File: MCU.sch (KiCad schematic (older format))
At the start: 36 parts, among them Q1 BSS138, SW1 SW_Push, U2 STM32F722RETx

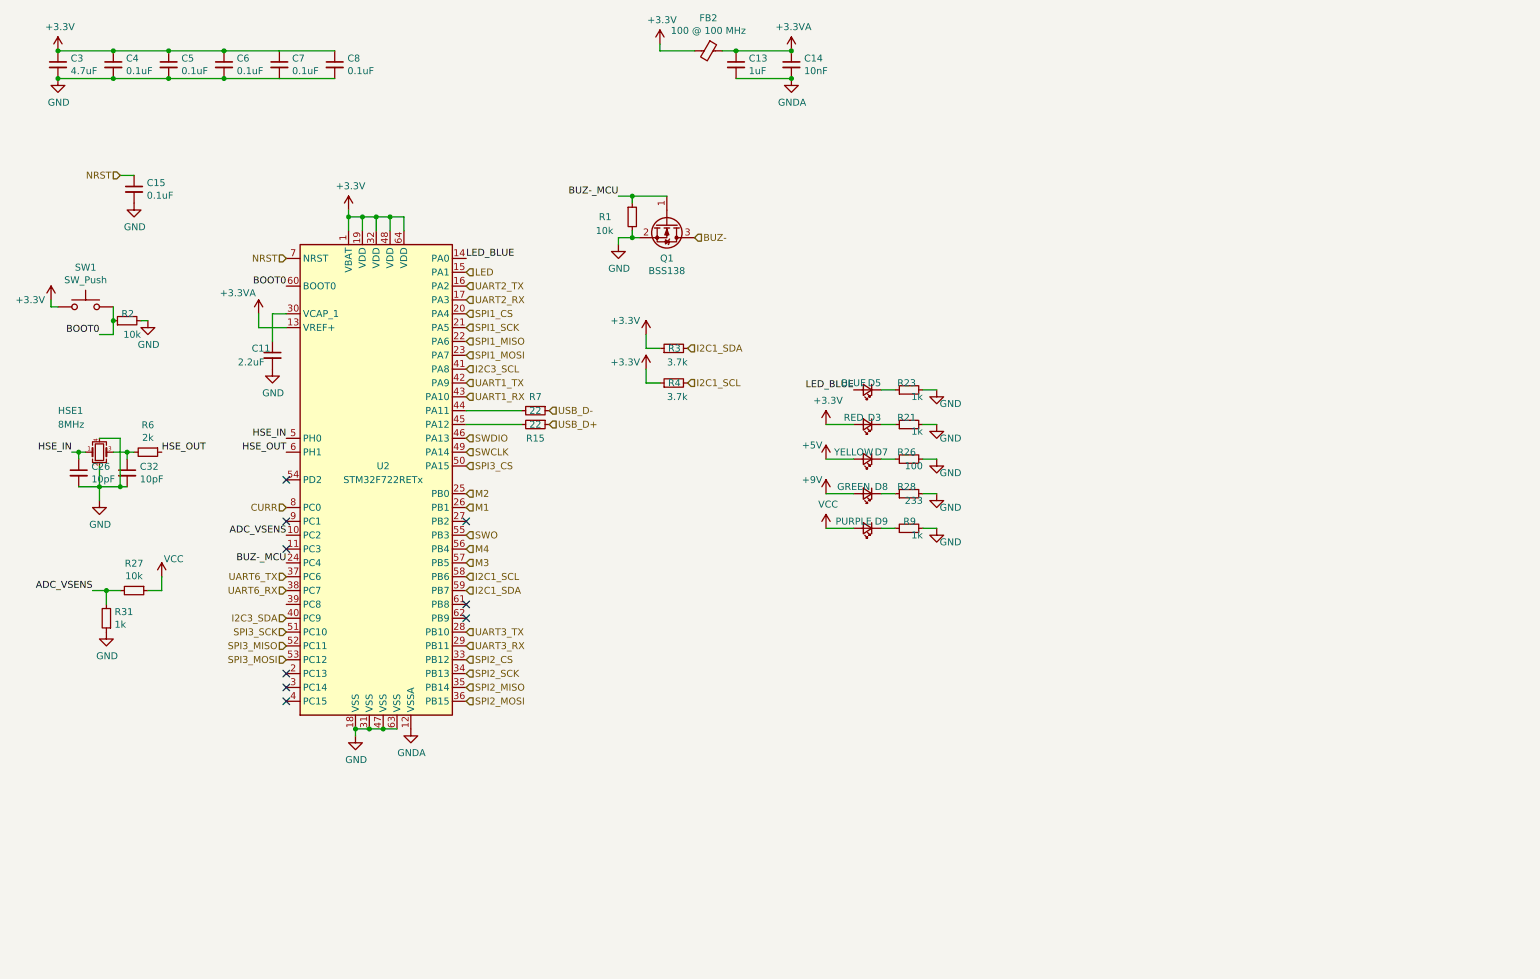
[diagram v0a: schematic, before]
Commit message: Updated the schematics to include pictures
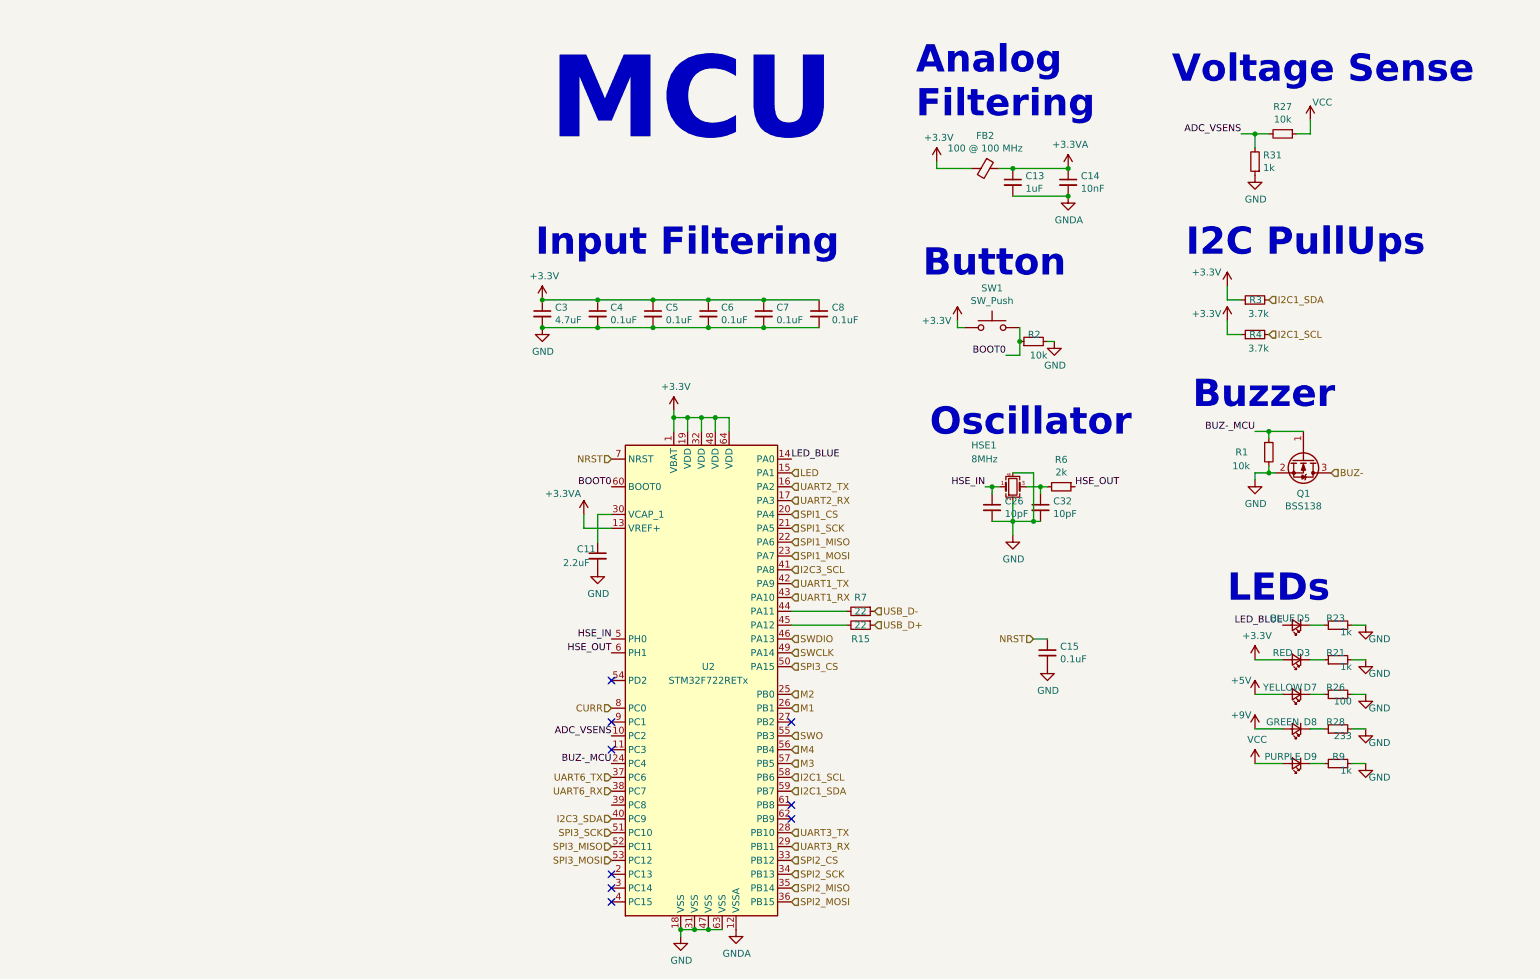
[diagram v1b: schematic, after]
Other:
- note added: "Analog\nFiltering"
- note added: "Button"
- note added: "Buzzer"
- note added: "I2C PullUps"
- note added: "Input Filtering"
- note added: "LEDs"
- note added: "MCU"
- note added: "Oscillator"
- note added: "Voltage Sense"
- moved on the sheet: C11, C13, C14, C15, C26, C3, C32, C4, C5, C6, C7, C8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

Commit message: Unknown changes
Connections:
- net D-: now reaches R15.2, U2.45 (PA12)
- net D+: now reaches R7.2, U2.44 (PA11)
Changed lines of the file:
@@
 Text Notes 4600 1550 0    591  ~ 118
 MCU
+Text Label 6500 4900 0    50   ~ 0
+D+
+Text Label 6500 5000 0    50   ~ 0
+D-
 $EndSCHEMATC
